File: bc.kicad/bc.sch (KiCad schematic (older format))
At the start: 74 parts, among them J1 Edge Connector, Q1 PMV48XP, SW1 SW_Push, U1 STM32L052C8Tx

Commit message: Layout keyboard half draft
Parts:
- C1, C11, C12, C13, C14, C2, C3, C4, C5, C6: footprint Capacitor_SMD:C_0603_1608Metric -> Capacitor_SMD:C_0402_1005Metric; LCSC C1623 -> C47339
- C10, C15, C16, C17, C18, C19, C20, C7, C8, C9: footprint Capacitor_SMD:C_0603_1608Metric -> Capacitor_SMD:C_0402_1005Metric; LCSC C14663 -> C1525
- C21: footprint (none) -> bc:keyboard
- D10: value LED -> LED_13
- D11: value LED -> LED_02A
- D12: value LED -> LED_06A
- D13: value LED -> LED_02B
- D14: value LED -> LED_06B
- D15: value LED -> LED_10
- D16: value LED -> LED_03A
- D17: value LED -> LED_07A
- D18: value LED -> LED_03B
- D19: value LED -> LED_07B
- D20: value LED -> LED_11
- D21: value LED -> LED_04A
- D22: value LED -> LED_08A
- D23: value LED -> LED_04B
- D24: value LED -> LED_08B
- D25: value LED -> LED_12
- D5: value LED -> LED_01A
- D6: value LED -> LED_05A
- D7: value LED -> LED_01B
- D8: value LED -> LED_05B
- D9: value LED -> LED_09
- R1, R10, R11, R12, R13, R14, R15, R16, R2, R3, R4, R5, R6, R7, R8, R9: footprint Resistor_SMD:R_0603_1608Metric -> Resistor_SMD:R_0402_1005Metric; LCSC C25804 -> C25744
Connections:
- net GND: now also TP1.1, TP3.1, TP4.1
- net LED_C3: now also TP5.1
- net at C1.2, C2.2, D1.1 (K)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: now also TP2.1
- no-connect marks 7 -> 2
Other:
- note added: "LED_XX_XXX"
- moved on the sheet: D10, D11, D12, D13, D14, D15, D16, D17, D18, D19, D20, D21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

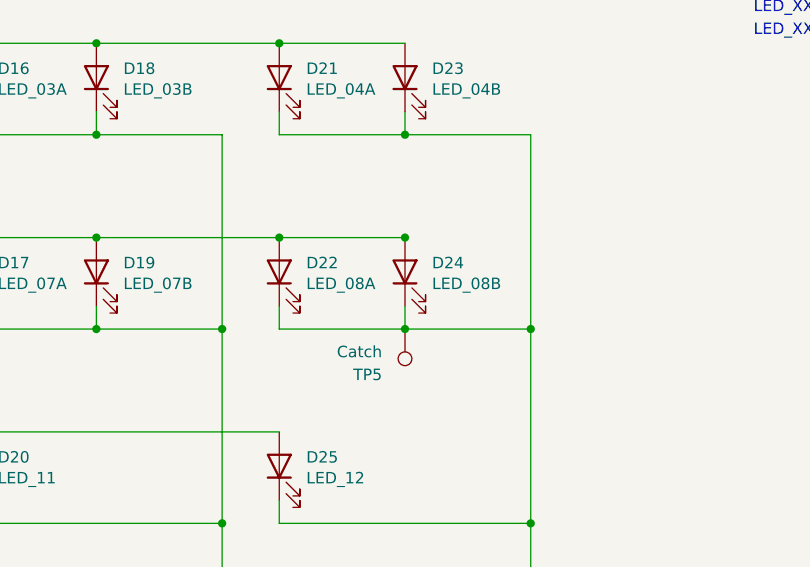
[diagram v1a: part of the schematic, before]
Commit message: Block as much light as possible between keys
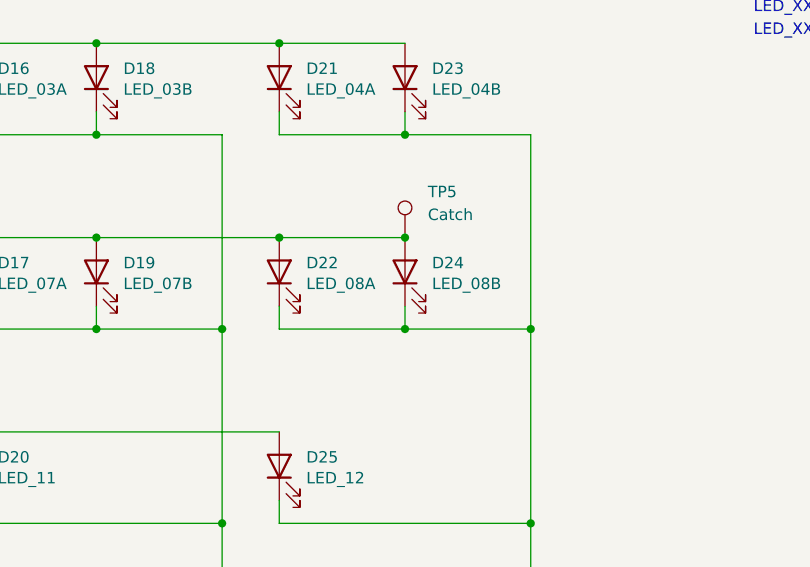
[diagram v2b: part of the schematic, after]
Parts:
- BT1: footprint Battery:BatteryHolder_Keystone_3002_1x2032 -> bc:BatteryHolder_Keystone_3002_1x2032
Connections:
- net LED_C3: no longer TP5.1
- net at C3.2, C4.2, D12.2 (A)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: now also TP5.1
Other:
- moved on the sheet: TP5
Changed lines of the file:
@@
 F 0 "BT1" H 4968 3796 50  0000 L CNN
 F 1 "CR2032" H 4968 3705 50  0000 L CNN
-F 2 "Battery:BatteryHolder_Keystone_3002_1x2032" V 4850 3760 50  0001 C CNN
+F 2 "bc:BatteryHolder_Keystone_3002_1x2032" V 4850 3760 50  0001 C CNN
 F 3 "https://datasheet.lcsc.com/szlcsc/1912111437_Keystone-3002TR_C238099.pdf" V 4850 3760 50  0001 C CNN
 F 4 "C238099" H 4850 3700 50  0001 C CNN "LCSC"
@@
 $EndComp
 $Comp
-L Connector:TestPoint TP2
-U 1 1 60256A01
-P 2450 4750
-F 0 "TP2" H 2500 4950 50  0000 L CNN
-F 1 "Catch" H 2500 4850 50  0000 L CNN
-F 2 "bc:test_point" H 2650 4750 50  0001 C CNN
-F 3 "https://datasheet.lcsc.com/szlcsc/1810151521_Keystone-5019_C238131.pdf" H 2650 4750 50  0001 C CNN
-F 4 "C238131" H 2450 4750 50  0001 C CNN "LCSC"
-	1    2450 4750
-	1    0    0    -1
-$EndComp
-$Comp
 L Connector:TestPoint TP5
 U 1 1 602646C7
-P 6300 6000
-F 0 "TP5" H 6400 6200 50  0000 L CNN
-F 1 "Catch" H 6400 6100 50  0000 L CNN
-F 2 "bc:test_point" H 6500 6000 50  0001 C CNN
-F 3 "https://datasheet.lcsc.com/szlcsc/1810151521_Keystone-5019_C238131.pdf" H 6500 6000 50  0001 C CNN
-F 4 "C238131" H 6300 6000 50  0001 C CNN "LCSC"
-	1    6300 6000
-	-1   0    0    1
+P 6300 5600
+F 0 "TP5" H 6400 5800 50  0000 L CNN
+F 1 "Catch" H 6400 5700 50  0000 L CNN
+F 2 "bc:test_point" H 6500 5600 50  0001 C CNN
+F 3 "https://datasheet.lcsc.com/szlcsc/1810151521_Keystone-5019_C238131.pdf" H 6500 5600 50  0001 C CNN
+F 4 "C238131" H 6300 5600 50  0001 C CNN "LCSC"
+	1    6300 5600
+	1    0    0    -1
 $EndComp
 $Comp
@@
 	1    0    0    -1
 $EndComp
+$Comp
+L Connector:TestPoint TP2
+U 1 1 60256A01
+P 2450 4750
+F 0 "TP2" H 2500 4950 50  0000 L CNN
+F 1 "Catch" H 2500 4850 50  0000 L CNN
+F 2 "bc:test_point" H 2650 4750 50  0001 C CNN
+F 3 "https://datasheet.lcsc.com/szlcsc/1810151521_Keystone-5019_C238131.pdf" H 2650 4750 50  0001 C CNN
+F 4 "C238131" H 2450 4750 50  0001 C CNN "LCSC"
+	1    2450 4750
+	1    0    0    -1
+$EndComp

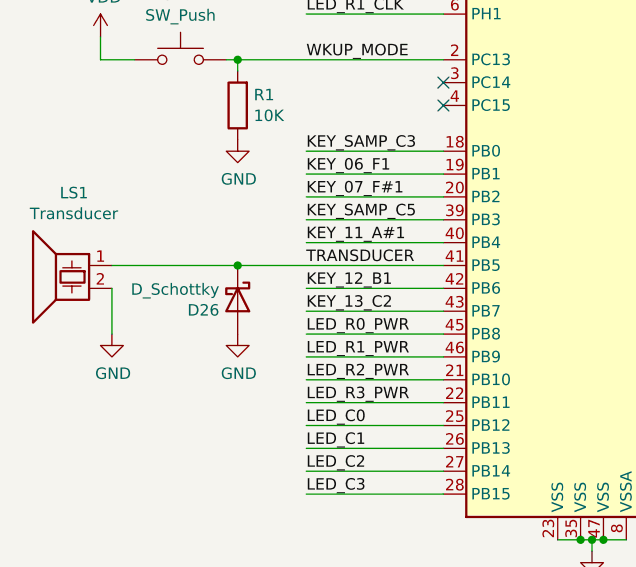
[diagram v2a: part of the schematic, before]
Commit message: Attempt pasta plate routing on the front
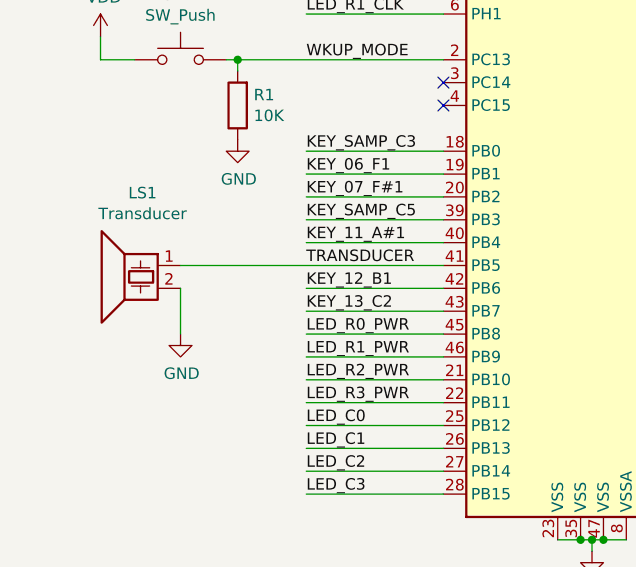
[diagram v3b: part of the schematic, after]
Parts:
- removed D26: D_Schottky, Diode_SMD:D_SOD-123, symbol Device:D_Schottky
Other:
- moved on the sheet: LS1
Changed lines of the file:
@@
 L Device:Speaker_Crystal LS1
 U 1 1 5FCC75DB
-P 750 2800
-F 0 "LS1" H 716 3117 50  0000 C CNN
-F 1 "Transducer" H 716 3026 50  0000 C CNN
-F 2 "bc:transducer" H 715 2750 50  0001 C CNN
-F 3 "https://www.puiaudio.com/media/SpecSheet/SMT-0940-T-3V-R.pdf" H 715 2750 50  0001 C CNN
-F 4 "668-1538-1-ND" H 750 2800 50  0001 C CNN "Digi-Key"
-	1    750  2800
+P 1050 2800
+F 0 "LS1" H 1016 3117 50  0000 C CNN
+F 1 "Transducer" H 1016 3026 50  0000 C CNN
+F 2 "bc:transducer" H 1015 2750 50  0001 C CNN
+F 3 "https://www.puiaudio.com/media/SpecSheet/SMT-0940-T-3V-R.pdf" H 1015 2750 50  0001 C CNN
+F 4 "668-1538-1-ND" H 1050 2800 50  0001 C CNN "Digi-Key"
+	1    1050 2800
 	-1   0    0    -1
 $EndComp
@@
 L power:GND #PWR02
 U 1 1 5FCCA8BC
-P 950 3100
-F 0 "#PWR02" H 950 2850 50  0001 C CNN
-F 1 "GND" H 955 2927 50  0000 C CNN
-F 2 "" H 950 3100 50  0001 C CNN
-F 3 "" H 950 3100 50  0001 C CNN
-	1    950  3100
+P 1250 3100
+F 0 "#PWR02" H 1250 2850 50  0001 C CNN
+F 1 "GND" H 1255 2927 50  0000 C CNN
+F 2 "" H 1250 3100 50  0001 C CNN
+F 3 "" H 1250 3100 50  0001 C CNN
+	1    1250 3100
 	1    0    0    -1
 $EndComp
 Wire Wire Line
-	950  3100 950  2900
-Wire Wire Line
-	950  2800 1500 2800
+	1250 3100 1250 2900
 Text Label 1800 2800 0    50   ~ 0
 TRANSDUCER
@@
 	1    0    0    -1
 $EndComp
-$Comp
-L Device:D_Schottky D26
-U 1 1 5FE957FC
-P 1500 2950
-F 0 "D26" V 1546 2870 50  0000 R CNN
-F 1 "D_Schottky" V 1455 2870 50  0000 R CNN
-F 2 "Diode_SMD:D_SOD-123" H 1500 2950 50  0001 C CNN
-F 3 "https://datasheet.lcsc.com/szlcsc/Changjiang-Electronics-Tech-CJ-B5819W_C8598.pdf" H 1500 2950 50  0001 C CNN
-F 4 " C8598" H 1500 2950 50  0001 C CNN "LCSC"
-	1    1500 2950
-	0    1    1    0
-$EndComp
-Connection ~ 1500 2800
-Wire Wire Line
-	1500 2800 2400 2800
-$Comp
-L power:GND #PWR0101
-U 1 1 5FF0614C
-P 1500 3100
-F 0 "#PWR0101" H 1500 2850 50  0001 C CNN
-F 1 "GND" H 1505 2927 50  0000 C CNN
-F 2 "" H 1500 3100 50  0001 C CNN
-F 3 "" H 1500 3100 50  0001 C CNN
-	1    1500 3100
-	1    0    0    -1
-$EndComp
 Text Notes 7825 4625 0    50   ~ 0
 LED_XX_XXX
@@
 $EndComp
 Connection ~ 6300 5600
+Wire Wire Line
+	1250 2800 2400 2800
 $EndSCHEMATC
